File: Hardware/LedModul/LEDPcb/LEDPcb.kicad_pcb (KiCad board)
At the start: 2 copper layers, 74.9 x 74.9 mm, 31 parts, among them J1 Conn_01x01_Pin, J2 Conn_01x01_Pin

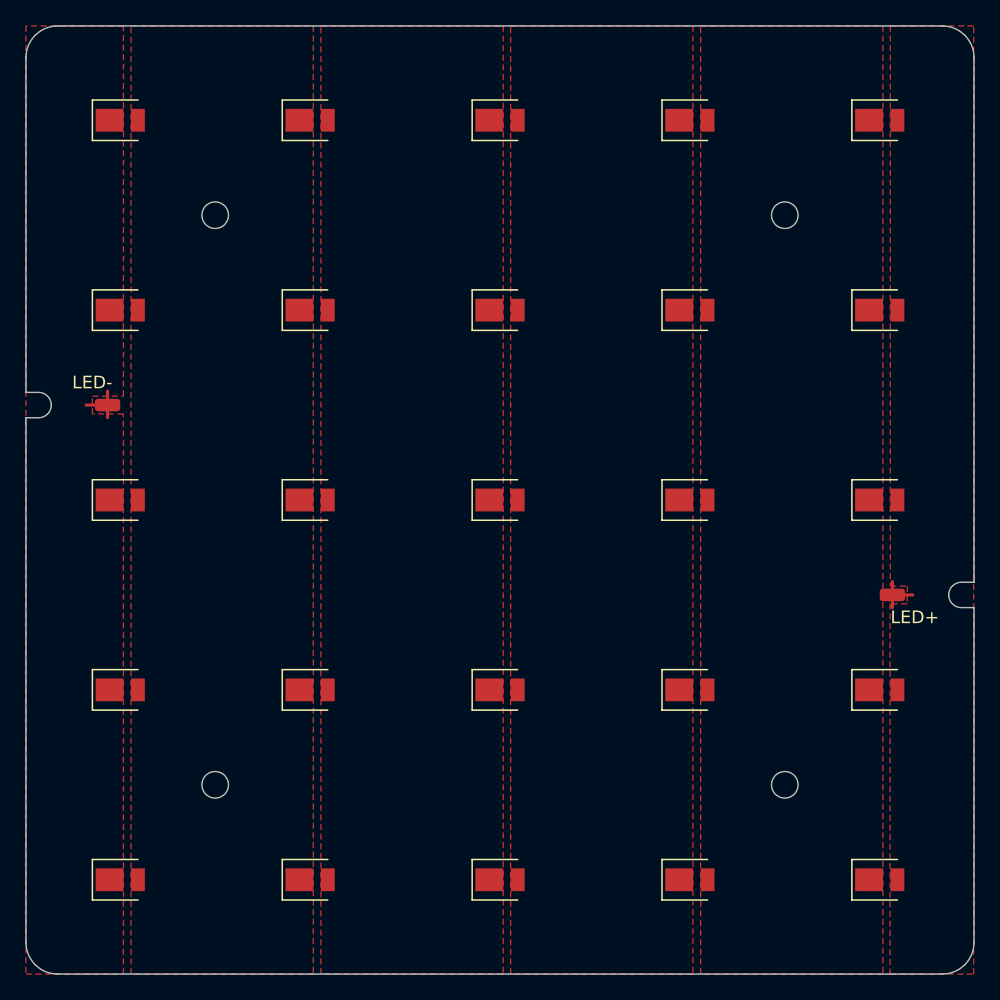
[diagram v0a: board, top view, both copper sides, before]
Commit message: added panel
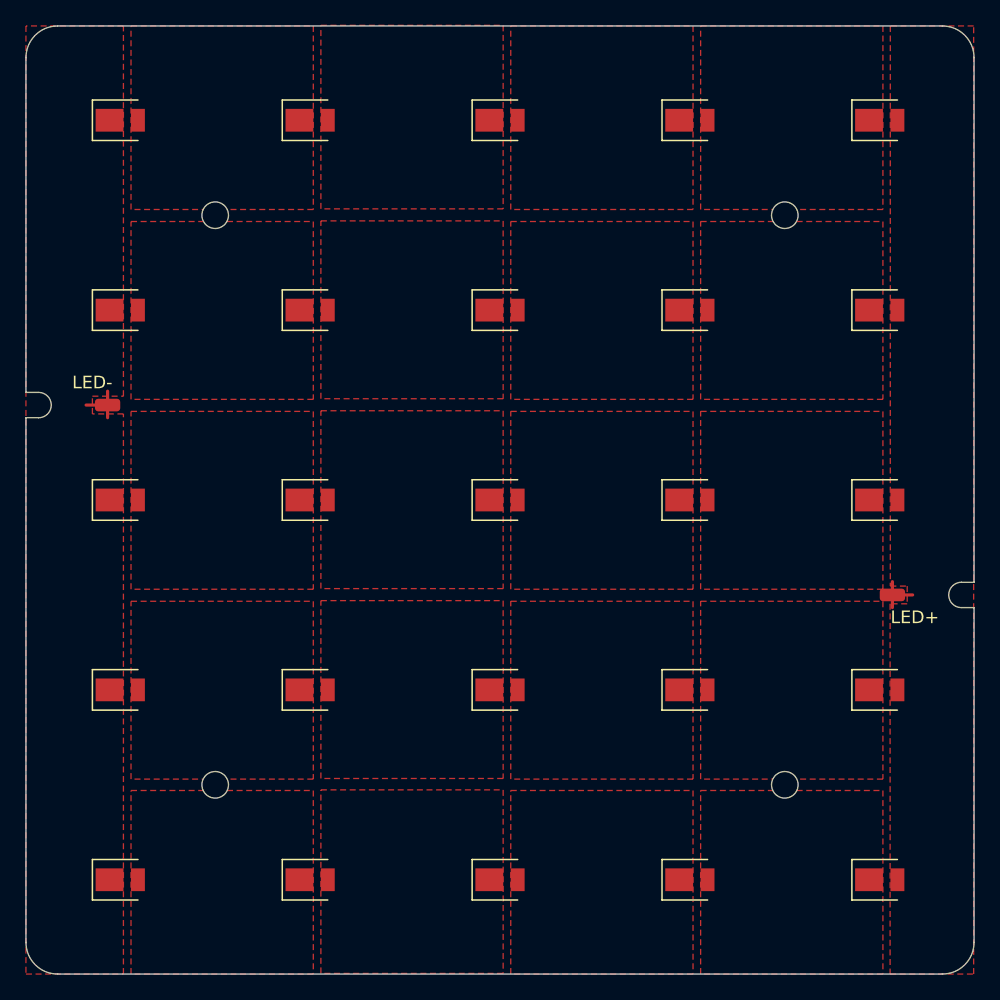
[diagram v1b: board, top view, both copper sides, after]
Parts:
- moved D1 60.0 mm to (107.5, 112.5)
- moved D5 60.0 mm to (107.5, 52.5)
- moved D2 30.0 mm to (107.5, 97.5)
- moved D4 30.0 mm to (107.5, 67.5)
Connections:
- D11 pad 1: Net-(D10-A) -> Net-(D11-K)
- D12 pad 1: Net-(D10-A) -> Net-(D12-K)
- D12 pad 2: Net-(D11-A) -> Net-(D12-A)
- D13 pad 1: Net-(D10-A) -> Net-(D13-K)
- D13 pad 2: Net-(D11-A) -> Net-(D13-A)
- D14 pad 1: Net-(D10-A) -> Net-(D14-K)
- D14 pad 2: Net-(D11-A) -> Net-(D14-A)
- D15 pad 2: Net-(D11-A) -> Net-(D15-A)
- D17 pad 1: Net-(D11-A) -> Net-(D12-A)
- D17 pad 2: Net-(D16-A) -> Net-(D17-A)
- D18 pad 1: Net-(D11-A) -> Net-(D13-A)
- D18 pad 2: Net-(D16-A) -> Net-(D18-A)
- D19 pad 1: Net-(D11-A) -> Net-(D14-A)
- D19 pad 2: Net-(D16-A) -> Net-(D19-A)
- D2 pad 2: Net-(D1-A) -> Net-(D2-A)
- D20 pad 1: Net-(D11-A) -> Net-(D15-A)
- D20 pad 2: Net-(D16-A) -> Net-(D20-A)
- D22 pad 1: Net-(D16-A) -> Net-(D17-A)
- D23 pad 1: Net-(D16-A) -> Net-(D18-A)
- D24 pad 1: Net-(D16-A) -> Net-(D19-A)
- D25 pad 1: Net-(D16-A) -> Net-(D20-A)
- D3 pad 2: Net-(D1-A) -> Net-(D3-A)
- D4 pad 2: Net-(D1-A) -> Net-(D4-A)
- D5 pad 2: Net-(D1-A) -> Net-(D5-A)
- D6 pad 1: Net-(D1-A) -> Net-(D5-A)
- D6 pad 2: Net-(D10-A) -> Net-(D11-K)
- D7 pad 1: Net-(D1-A) -> Net-(D4-A)
- D7 pad 2: Net-(D10-A) -> Net-(D12-K)
- D8 pad 1: Net-(D1-A) -> Net-(D3-A)
- D8 pad 2: Net-(D10-A) -> Net-(D13-K)
- D9 pad 1: Net-(D1-A) -> Net-(D2-A)
- D9 pad 2: Net-(D10-A) -> Net-(D14-K)
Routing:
- added copper zone on F.Cu, net Net-(D11-K)
- added copper zone on F.Cu, net Net-(D12-A)
- added copper zone on F.Cu, net Net-(D12-K)
- added copper zone on F.Cu, net Net-(D13-A)
- added copper zone on F.Cu, net Net-(D13-K)
- added copper zone on F.Cu, net Net-(D14-A)
- added copper zone on F.Cu, net Net-(D14-K)
- added copper zone on F.Cu, net Net-(D15-A)
- added copper zone on F.Cu, net Net-(D17-A)
- added copper zone on F.Cu, net Net-(D18-A)
- added copper zone on F.Cu, net Net-(D19-A)
- added copper zone on F.Cu, net Net-(D2-A)
- added copper zone on F.Cu, net Net-(D20-A)
- added copper zone on F.Cu, net Net-(D3-A)
- added copper zone on F.Cu, net Net-(D4-A)
- added copper zone on F.Cu, net Net-(D5-A)

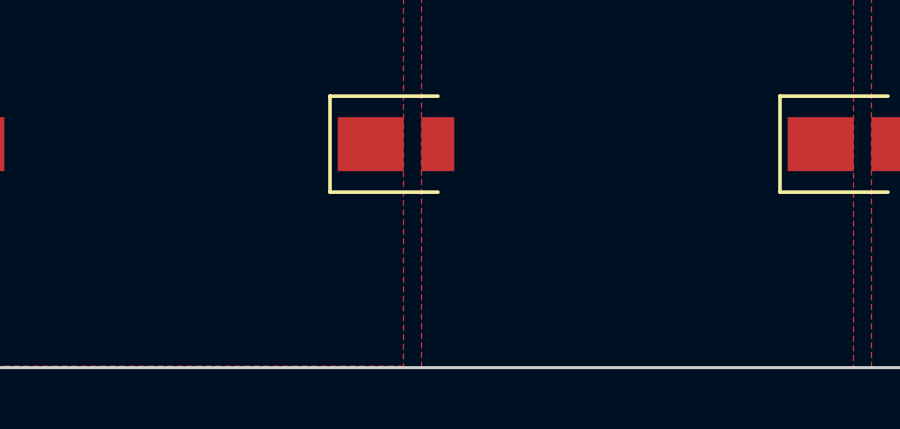
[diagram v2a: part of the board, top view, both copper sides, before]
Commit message: added Pcb name and version to silkscreen
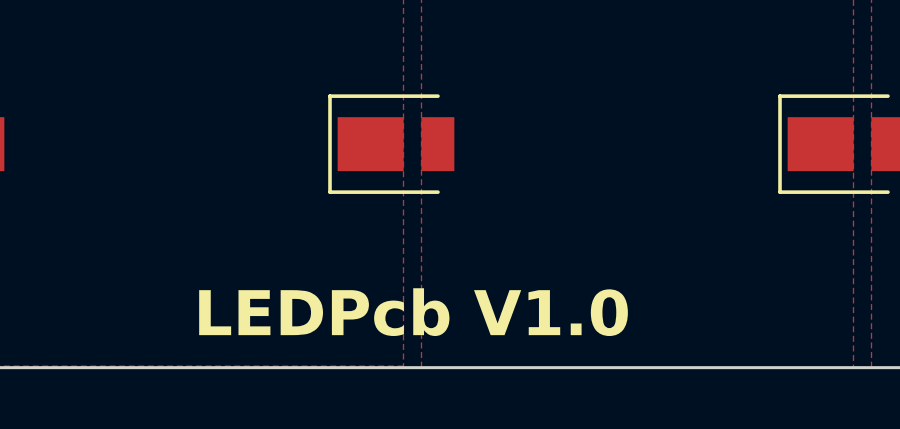
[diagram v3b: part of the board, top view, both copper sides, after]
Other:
- board text added: "LEDPcb V1.0"
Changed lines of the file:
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@@
     (effects (font (size 1 1) (thickness 0.15)) (justify left bottom))
+  )
+  (gr_text "LEDPcb V1.0" (at 130.7 119.1) (layer "F.SilkS")
+    (effects (font (size 1.5 1.5) (thickness 0.3) bold) (justify left bottom))
   )
   (dimension (type aligned) (layer "Dwgs.User")

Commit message: V1.1
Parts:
- added J3: Conn_01x01_Pin, Bergi:S9141-45R, F.Cu at (130.4, 75.5)
- added J4: Conn_01x01_Pin, Bergi:S9141-45R, F.Cu at (144.5, 89.6)
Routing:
- net /LED+: track 3.65 -> 31.3 mm
- net /LED-: track 3.80 -> 28.9 mm
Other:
- board text added: "LEDPcb V1.1"
- board text removed: "LEDPcb V1.0"
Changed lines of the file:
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@@
+    )
+  )
+  (footprint "Bergi:S9141-45R" (layer "F.Cu")
+    (at 144.5 89.6)
+    (property "Sheetfile" "LEDPcb.kicad_sch")
+    (property "Sheetname" "")
+    (property "ki_description" "Generic connector, single row, 01x01, script generated")
+    (property "ki_keywords" "connector")
+    (attr smd)
+    (fp_text reference "J4" (at -0.04 -1.47 unlocked) (layer "F.SilkS") hide
+        (effects (font (size 1 1) (thickness 0.1)))
+    )
+    (fp_text value "Conn_01x01_Pin" (at -0.04 0.03 unlocked) (layer "F.Fab") hide
+        (effects (font (size 1 1) (thickness 0.15)))
+    )
+    (fp_text user "${REFERENCE}" (at -0.04 1.53 unlocked) (layer "F.Fab") hide
+        (effects (font (size 1 1) (thickness 0.15)))
+    )
+    (pad "" np_thru_hole circle (at 0 0) (size 3 3) (drill 3) (layers "F&B.Cu" "*.Mask"))
+    (pad "1" smd trapezoid (at 0 -2.35 180) (size 1.608 1) (rect_delta 0 0.342) (layers "F.Cu" "F.Paste" "F.Mask")
+      (net 6 "/LED+") (pinfunction "Pin_1") (pintype "passive"))
+    (pad "1" smd trapezoid (at 0 2.35) (size 1.608 1) (rect_delta 0 0.342) (layers "F.Cu" "F.Paste" "F.Mask")
+      (net 6 "/LED+") (pinfunction "Pin_1") (pintype "passive"))
+    (model "D:/workspace/kicad_7/bergiKicadLib/3D_Model/Bergi/S9141-45R.stp"
+      (offset (xyz 0 0 0))
+      (scale (xyz 1 1 1))
+      (rotate (xyz -90 0 0))
     )
   )
@@
     )
   )
+  (footprint "Bergi:S9141-45R" (layer "F.Cu")
+    (at 130.4 75.5)
+    (property "Sheetfile" "LEDPcb.kicad_sch")
+    (property "Sheetname" "")
+    (property "ki_description" "Generic connector, single row, 01x01, script generated")
+    (property "ki_keywords" "connector")
+    (attr smd)
+    (fp_text reference "J3" (at -0.04 -1.47 unlocked) (layer "F.SilkS") hide
+        (effects (font (size 1 1) (thickness 0.1)))
+    )
+    (fp_text value "Conn_01x01_Pin" (at -0.04 0.03 unlocked) (layer "F.Fab") hide
+        (effects (font (size 1 1) (thickness 0.15)))
+    )
+    (fp_text user "${REFERENCE}" (at -0.04 1.53 unlocked) (layer "F.Fab") hide
+        (effects (font (size 1 1) (thickness 0.15)))
+    )
+    (pad "" np_thru_hole circle (at 0 0) (size 3 3) (drill 3) (layers "F&B.Cu" "*.Mask"))
+    (pad "1" smd trapezoid (at 0 -2.35 180) (size 1.608 1) (rect_delta 0 0.342) (layers "F.Cu" "F.Paste" "F.Mask")
+      (net 1 "/LED-") (pinfunction "Pin_1") (pintype "passive"))
+    (pad "1" smd trapezoid (at 0 2.35) (size 1.608 1) (rect_delta 0 0.342) (layers "F.Cu" "F.Paste" "F.Mask")
+      (net 1 "/LED-") (pinfunction "Pin_1") (pintype "passive"))
+    (model "D:/workspace/kicad_7/bergiKicadLib/3D_Model/Bergi/S9141-45R.stp"
+      (offset (xyz 0 0 0))
+      (scale (xyz 1 1 1))
+      (rotate (xyz -90 0 0))
+    )
+  )
   (footprint "Bergi:LED_J2835" locked (layer "F.Cu")
     (at 122.45 67.55)
@@
     (effects (font (size 1 1) (thickness 0.15)) (justify left bottom))
   )
-  (gr_text "LEDPcb V1.0" (at 130.7 119.1) (layer "F.SilkS")
+  (gr_text "LED+" (at 140.95 88 -90) (layer "F.SilkS")
+    (effects (font (size 1 1) (thickness 0.15)) (justify left bottom))
+  )
+  (gr_text "LED-" (at 134 77 90) (layer "F.SilkS")
+    (effects (font (size 1 1) (thickness 0.15)) (justify left bottom))
+  )
+  (gr_text "LEDPcb V1.1" (at 130.7 119.1) (layer "F.SilkS")
     (effects (font (size 1.5 1.5) (thickness 0.3) bold) (justify left bottom))
   )
@@
     (style (thickness 0.15) (arrow_length 1.27) (text_position_mode 0) (extension_height 0.58642) (extension_offset 0.5) keep_text_aligned)
   )
+  (segment (start 108.65 74.8) (end 107.6 73.75) (width 1) (layer "F.Cu") (net 1))
+  (segment (start 107.55 76.35) (end 108.65 75.25) (width 1) (layer "F.Cu") (net 1))
+  (segment (start 127.35 75) (end 108.65 75) (width 1) (layer "F.Cu") (net 1))
+  (segment (start 127.3 75.45) (end 127.35 75.4) (width 1) (layer "F.Cu") (net 1))
   (segment (start 106.45 75.05) (end 106.45 76.05) (width 0.25) (layer "F.Cu") (net 1))
   (segment (start 106.45 75.05) (end 106.45 73.95) (width 0.25) (layer "F.Cu") (net 1))
+  (segment (start 108.65 75) (end 108.65 74.8) (width 1) (layer "F.Cu") (net 1))
+  (segment (start 106.1 76.35) (end 107.55 76.35) (width 1) (layer "F.Cu") (net 1))
   (segment (start 106.45 75.05) (end 104.75 75.05) (width 0.25) (layer "F.Cu") (net 1))
+  (segment (start 107.6 73.75) (end 106.65 73.75) (width 1) (layer "F.Cu") (net 1))
+  (segment (start 127.35 75.4) (end 127.35 75) (width 1) (layer "F.Cu") (net 1))
+  (segment (start 108.65 75.25) (end 108.65 75) (width 1) (layer "F.Cu") (net 1))
   (segment (start 168.45 90.05) (end 170.05 90.05) (width 0.25) (layer "F.Cu") (net 6))
+  (segment (start 165.85 90.15) (end 165.9 90.15) (width 1) (layer "F.Cu") (net 6))
+  (segment (start 167.25 91.3) (end 168.9 91.3) (width 1) (layer "F.Cu") (net 6))
+  (segment (start 165.85 90.15) (end 166.1 90.15) (width 1) (layer "F.Cu") (net 6))
+  (segment (start 165.9 90.15) (end 167.25 88.8) (width 1) (layer "F.Cu") (net 6))
+  (segment (start 169.3 88.8) (end 169.75 88.35) (width 1) (layer "F.Cu") (net 6))
+  (segment (start 166.1 90.15) (end 167.25 91.3) (width 1) (layer "F.Cu") (net 6))
+  (segment (start 165.85 90.15) (end 147.05 90.15) (width 1) (layer "F.Cu") (net 6))
   (segment (start 168.45 90.05) (end 168.45 89) (width 0.25) (layer "F.Cu") (net 6))
+  (segment (start 167.25 88.8) (end 169.3 88.8) (width 1) (layer "F.Cu") (net 6))
   (segment (start 168.45 90.05) (end 168.45 91.05) (width 0.25) (layer "F.Cu") (net 6))
+  (segment (start 168.9 91.3) (end 169.4 91.8) (width 1) (layer "F.Cu") (net 6))
   (zone (net 18) (net_name "Net-(D15-A)") (layer "F.Cu") (hatch edge 0.5)
     (priority 1)
@@
         (xy 137.7 105.45)
         (xy 137.7 119.95)
+      )
+    )
+  )
+  (zone (net 1) (net_name "/LED-") (layer "F.Cu") (hatch edge 0.5)
+    (priority 2)
+    (connect_pads yes (clearance 0.5))
+    (min_thickness 0.25) (filled_areas_thickness no)
+    (fill yes (thermal_gap 0.5) (thermal_bridge_width 0.5))
+    (polygon
+      (pts
+        (xy 131.45 78.35)
+        (xy 133.05 76.75)
+        (xy 133.05 74.2)
+        (xy 131.45 72.6)
+        (xy 129 72.6)
+        (xy 126.3 75.3)
+        (xy 126.3 75.4)
+        (xy 129.25 78.35)
       )
     )
@@
       )
     )
+  )
+  (zone (net 6) (net_name "/LED+") (layer "F.Cu") (hatch edge 0.5)
+    (priority 2)
+    (connect_pads yes (clearance 0.5))
+    (min_thickness 0.25) (filled_areas_thickness no)
+    (fill yes (thermal_gap 0.5) (thermal_bridge_width 0.5))
+    (polygon
+      (pts
+        (xy 143.45 86.75)
+        (xy 141.85 88.35)
+        (xy 141.85 90.9)
+        (xy 143.45 92.5)
+        (xy 145.9 92.5)
+        (xy 148.6 89.8)
+        (xy 148.6 89.7)
+        (xy 145.65 86.75)
+      )
+    )
